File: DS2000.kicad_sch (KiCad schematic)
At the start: 56 parts, among them J1 USB-C, J3 USB wire, SW1 MUTE, SW2 DEAFEN, SW3 DISCONNECT, U1 USBLC6-2SC6, U2 AP2112K-3.3, U3 RP2350A, U4 W25Q32JVSS, U5 74AHCT1G125, Y1 12MHz

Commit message: feat: cost-down for one-sided JLC assembly
Move every assembled part to the top side so JLC can assemble the board
with Economic PCBA, and swap parts that have a JLC basic (no feeder fee)
or cheaper drop-in equivalent.

- remove the USB-C receptacle (J1) and its CC resistors (R1, R2): the USB
  cable is soldered to J3, which now feeds +5V directly
- remove the PTC fuse (F1): the host port limits the current
- D1/D2: SK6812MINI-E reverse-mount (bottom) -> WS2812B-2020-V6 on the
  top, inside the Choc V1 LED window; no more board cut-outs
- C21/C22 move to the top, between the keys, under the keycap overhang
- U2: AP2112K-3.3 (SOT-23-5) -> XC6206P332MR (SOT-23-3, basic)
- Y1: ABM8-272-T3 -> YXC X322512MSB4SI (basic), C17/C18 15p -> 33p
- C3-C5 -> CL05A475MP5NRNC (basic), R5 -> 0402WGF330JTCE (basic)
- U1 -> UMW USBLC6-2SC6, U4 -> W25Q16JVSSIQ (2 MB, same footprint)
- the changed nets rerouted with Freerouting, existing tracks locked
- STEP model for the WS2812B-2020, docs and renders updated

Co-Authored-By: Claude Opus 5.5 <noreply@anthropic.com>
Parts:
- removed F1: 500mA hold, Fuse:Fuse_1206_3216Metric, symbol Device:Polyfuse_Small
- removed J1: USB-C, Connector_USB:USB_C_Receptacle_HRO_TYPE-C-31-M-12, symbol Connector:USB_C_Receptacle_USB2.0_16P
- removed R1, R2: 5.1k, Resistor_SMD:R_0402_1005Metric, symbol Device:R_Small
- C17, C18: value 15p -> 33p; LCSC C1548 -> C1562; MPN 0402CG150J500NT -> 0402CG330J500NT
- C3, C4, C5: LCSC C82453 -> C23733; MPN GRM155R60J475ME47D -> CL05A475MP5NRNC; Manufacturer Murata -> Samsung Electro-Mechanics
- D1, D2: value SK6812MINI-E -> WS2812B-2020; footprint LED_SMD:LED_SK6812MINI-E_3.2x2.8mm_P1.5mm_ReverseMount -> LED_SMD:LED_WS2812B-2020_PLCC4_2.0x2.0mm; symbol LED:SK6812MINI-E -> LED:WS2812B-2020; LCSC C5149201 -> C52917434; MPN SK6812MINI-E -> WS2812B-2020-V6; Manufacturer Opsco -> Worldsemi
- R5: LCSC C138002 -> C25105; MPN RC0402FR-0733RL -> 0402WGF330JTCE; Manufacturer Yageo -> UNI-ROYAL
- U1: LCSC C7519 -> C2687116; Manufacturer STMicroelectronics -> UMW
- U2: value AP2112K-3.3 -> XC6206P332MR; footprint Package_TO_SOT_SMD:SOT-23-5 -> Package_TO_SOT_SMD:SOT-23-3; symbol Regulator_Linear:AP2112K-3.3 -> Regulator_Linear:XC6206PxxxMR; LCSC C51118 -> C5446; MPN AP2112K-3.3TRG1 -> XC6206P332MR-G; Manufacturer Diodes Inc -> Torex
- U4: LCSC C179173 -> C82317; MPN W25Q32JVSSIQ -> W25Q16JVSSIQ
- Y1: LCSC C20625731 -> C9002; MPN ABM8-272-T3 -> X322512MSB4SI; Manufacturer Abracon -> YXC
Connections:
- net VBUS is gone; now on net +5V: J3.1 (Pin_1)
- net +3V3: now also U2.2 (VO); no longer U2.5 (VOUT)
- net +5V: now also D1.4 (VDD), D2.4 (VDD); no longer D1.3 (VDD), D2.3 (VDD), U2.1 (VIN)
- net GND: now also D1.2 (VSS), D2.2 (VSS), U2.1 (GND); no longer D1.1 (VSS), D2.1 (VSS), U2.2 (GND)
- net at R10.2: now also D1.3 (DIN); no longer D1.2 (DIN)
- new net: D1.1 (DOUT), D2.3 (DIN)
- no-connect marks 30 -> 27
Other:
- note added: "D1 under mute, D2 under deafen, top side, in the switch LED window. Disconnect has no LED. 100n per LED."
- note added: "J3: the USB cable is soldered to these pads. No fuse: the host port limits the current. U1 next to J3, R3/R4 next to the RP2350."
- note added: "Key LEDs: 3.3 V -> 5 V level shift, WS2812B-2020"
- note added: "USB input (soldered cable) and ESD"
- note added: "XC6206: 200 mA, enough for the RP2350A and flash."
- note removed: "CC 5.1k: USB device (UFP). U1 at the connector, R3/R4 next to the RP2350. J3: optional soldered cable."
- note removed: "D1 under mute, D2 under deafen (reverse-mounted). Disconnect key has no LED. One 100n per LED."
- note removed: "EN tied to VIN: always on. 250 mV dropout."
- note removed: "Key LEDs: 3.3 V -> 5 V level shift, SK6812MINI-E"
- note removed: "USB-C input, fuse, ESD and wire pads"
- moved on the sheet: J3

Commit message: fix: U4 value matches the 2 MB flash
Co-Authored-By: Claude Opus 5.5 <noreply@anthropic.com>
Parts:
- U4: value W25Q32JVSS -> W25Q16JVSS
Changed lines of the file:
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@@
 			)
 		)
-		(property "Value" "W25Q32JVSS"
+		(property "Value" "W25Q16JVSS"
 			(at 86.36 210.82 0)
 			(show_name no)

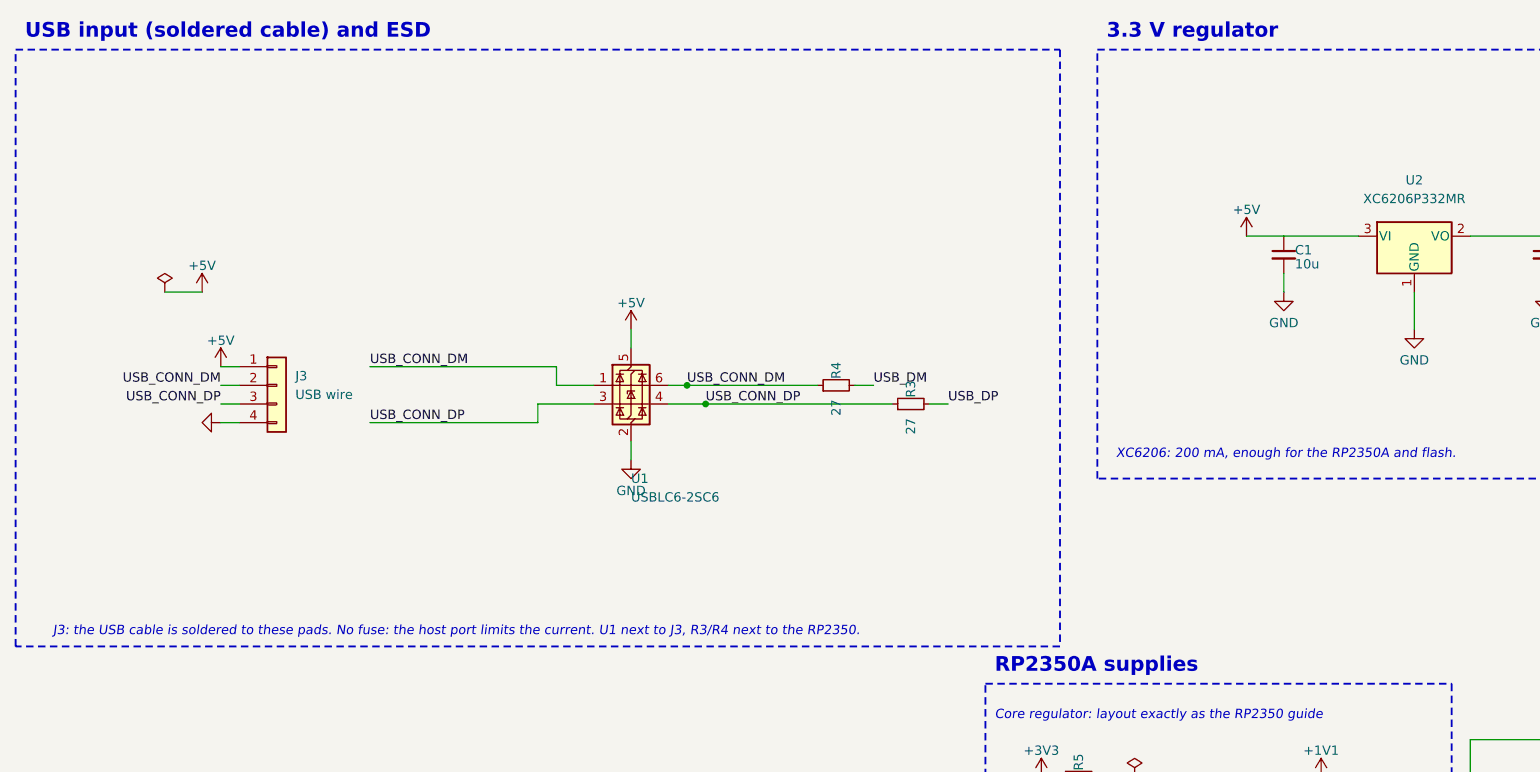
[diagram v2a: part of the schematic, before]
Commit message: fix: keep the USB-C footprint, hand-soldered instead of assembled
The cost-down removed J1 to keep JLC's assembly one-sided. The receptacle
only has to stay out of JLC's files for that, not off the board: J1 is back
in its place on the bottom, marked DNP and excluded from the BOM and the
placement file, to be soldered by hand after assembly. J3 stays as the
alternative for a soldered cable.

- J1's VBUS goes straight to +5V, like J3; there is still no fuse.
- R1/R2, the 5.1k CC pull-downs a USB-C host needs before it supplies 5 V,
  are back on the top side (basic part, assembled).
- J1's escape routing is main's; the +5V and D+ runs it displaced were
  rerouted around it.
- set_fields.py, README and design notes describe J1 as DNP.

ERC 0. DRC: 0 unconnected, 0 parity issues; the rest is the 13 known
text_thickness notes and the two library-mismatch notes (Y1, and J1 as
on main).

Co-Authored-By: Claude Opus 5.5 <noreply@anthropic.com>
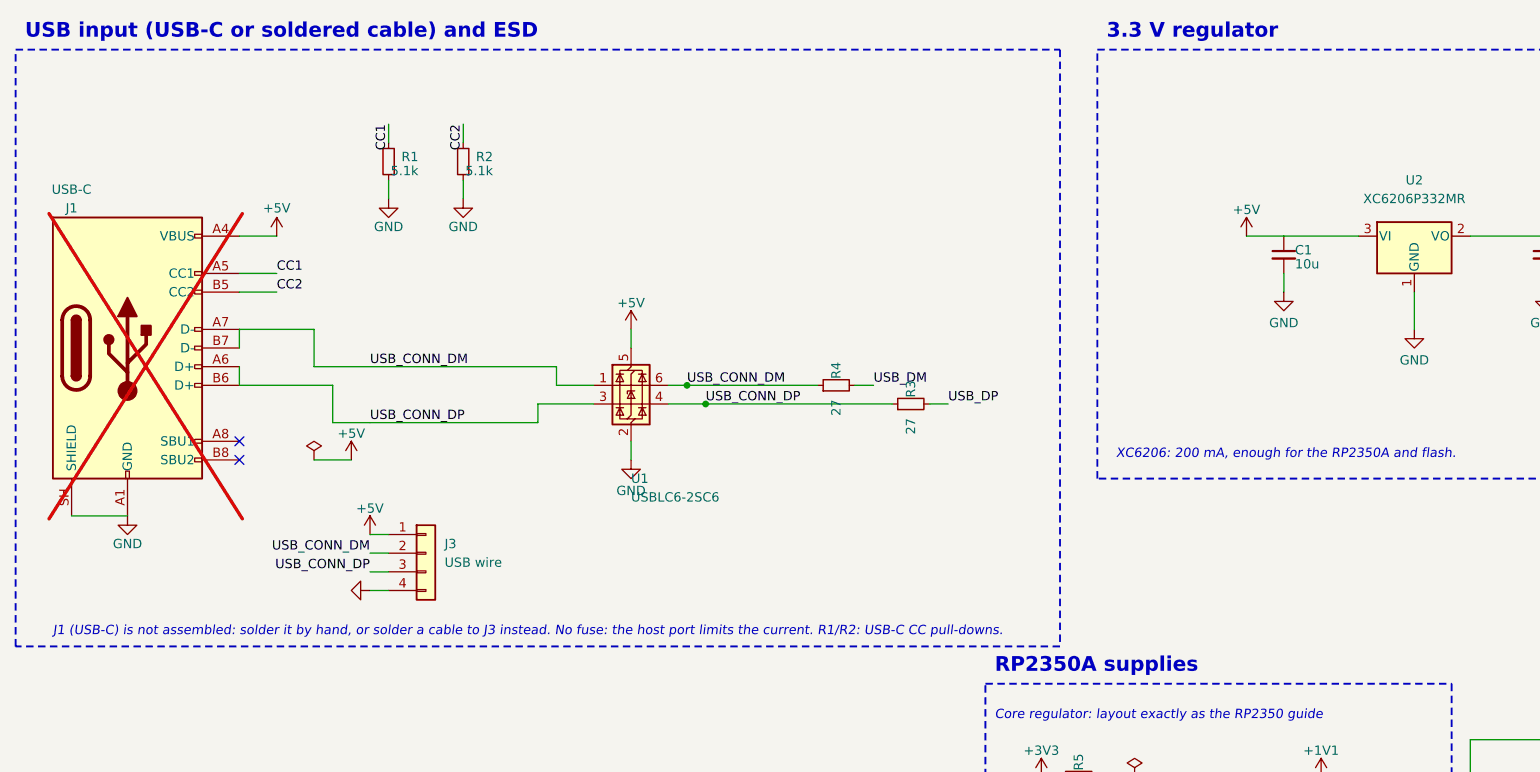
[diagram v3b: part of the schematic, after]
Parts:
- added J1: USB-C, Connector_USB:USB_C_Receptacle_HRO_TYPE-C-31-M-12, symbol Connector:USB_C_Receptacle_USB2.0_16P
- added R1, R2: 5.1k, Resistor_SMD:R_0402_1005Metric, symbol Device:R_Small
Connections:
- net +5V: now also J1.A4 (VBUS), J1.A9 (VBUS), J1.B4 (VBUS), J1.B9 (VBUS)
- net GND: now also J1.A1 (GND), J1.A12 (GND), J1.B1 (GND), J1.B12 (GND), J1.SH (SHIELD), R1.1, R2.1
- net USB_CONN_DM: now also J1.A7 (D-), J1.B7 (D-)
- net USB_CONN_DP: now also J1.A6 (D+), J1.B6 (D+)
- new net CC1: J1.A5 (CC1), R1.2
- new net CC2: J1.B5 (CC2), R2.2
- no-connect marks 27 -> 29
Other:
- note added: "J1 (USB-C) is not assembled: solder it by hand, or solder a cable to J3 instead. No fuse: the host port limits the current. R1/R2: USB-C CC pull-downs."
- note added: "USB input (USB-C or soldered cable) and ESD"
- note removed: "J3: the USB cable is soldered to these pads. No fuse: the host port limits the current. U1 next to J3, R3/R4 next to the RP2350."
- note removed: "USB input (soldered cable) and ESD"
- moved on the sheet: J3
